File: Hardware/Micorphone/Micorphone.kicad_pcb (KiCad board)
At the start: 2 copper layers, 14 x 28 mm, 7 parts, among them J1 LAMP1, U1 ICS-40618

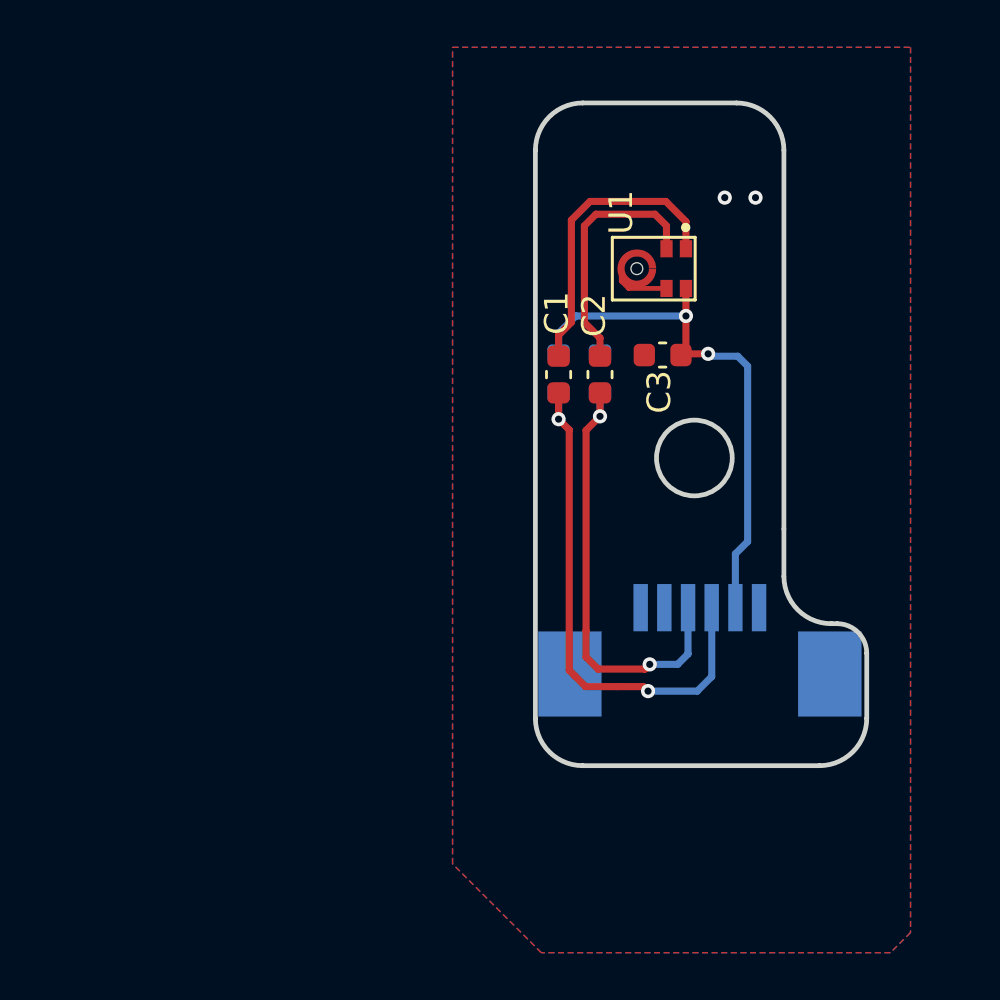
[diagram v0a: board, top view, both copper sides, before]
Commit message: Update hardware projects for Gerber generation
- Configure Gerber output directories for Microphone, QWIIC LEDs, and UNO Q Breakout projects.
- Update .gitignore to exclude Gerber and drill files.
- Refine PCB layouts and update versioning labels for production readiness.
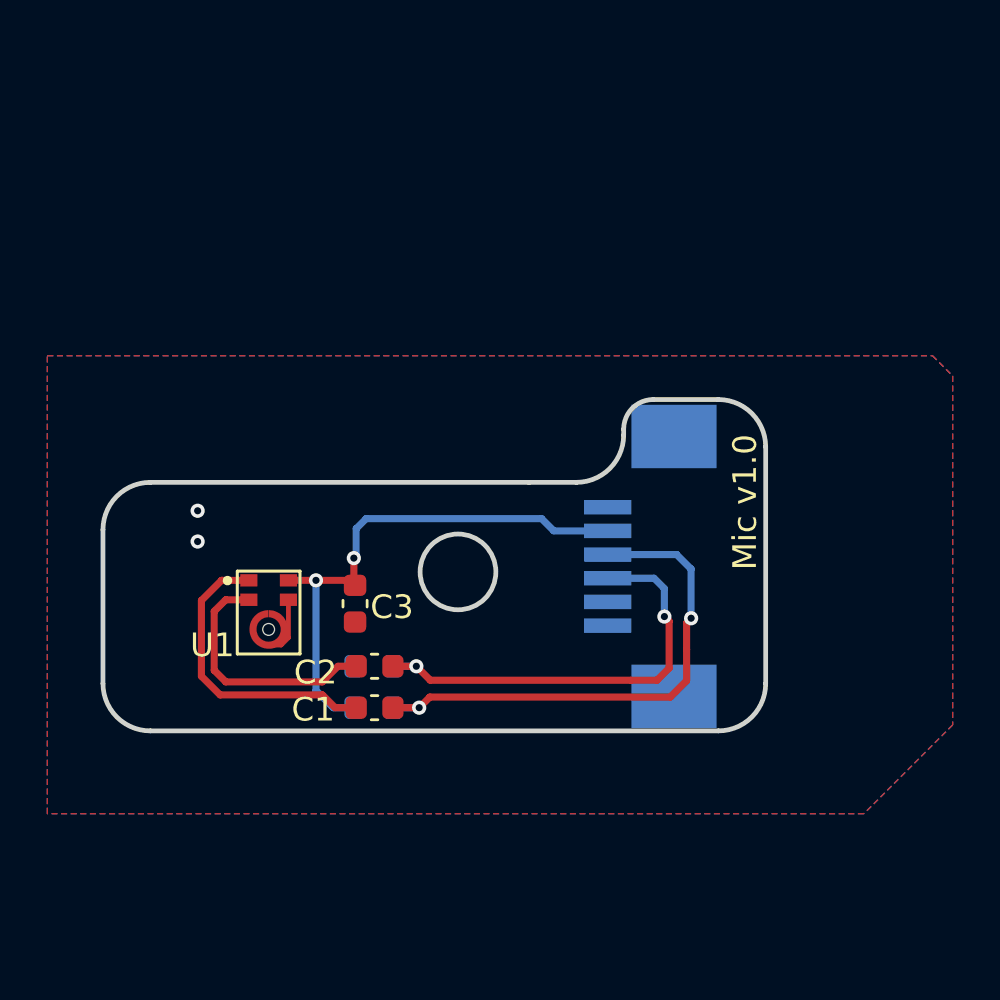
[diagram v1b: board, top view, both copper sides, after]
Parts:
- moved U1 21.8 mm to (89.2, 93.5), turned to 0 degrees
- moved C3 16.7 mm to (92.9, 93.2), turned to -90 degrees
- moved R1 16.1 mm to (93.7, 97.5), turned to 180 degrees
- moved C1 16.1 mm to (93.7, 97.5), turned to 0 degrees
- moved R2 15.6 mm to (93.7, 95.8), turned to 0 degrees
- moved C2 15.6 mm to (93.7, 95.8), turned to 0 degrees
- moved J1 4.12 mm to (105.4, 91.6), turned to -90 degrees
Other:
- board size 14 x 28 mm -> 28 x 14 mm
- board text added: "Mic v1.0"
